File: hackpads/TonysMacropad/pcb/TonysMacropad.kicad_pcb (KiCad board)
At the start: 2 copper layers, 81 x 61.9 mm, 21 parts, among them SW1 SW_Push_45deg, SW2 SW_Push_45deg, SW3 SW_Push_45deg, SW4 SW_Push_45deg, SW5 SW_Push_45deg, SW6 SW_Push_45deg, SW7 SW_Push_45deg, SW8 SW_Push_45deg, SW9 SW_Push_45deg, U1 Seeed Studio XIAO SAMD21

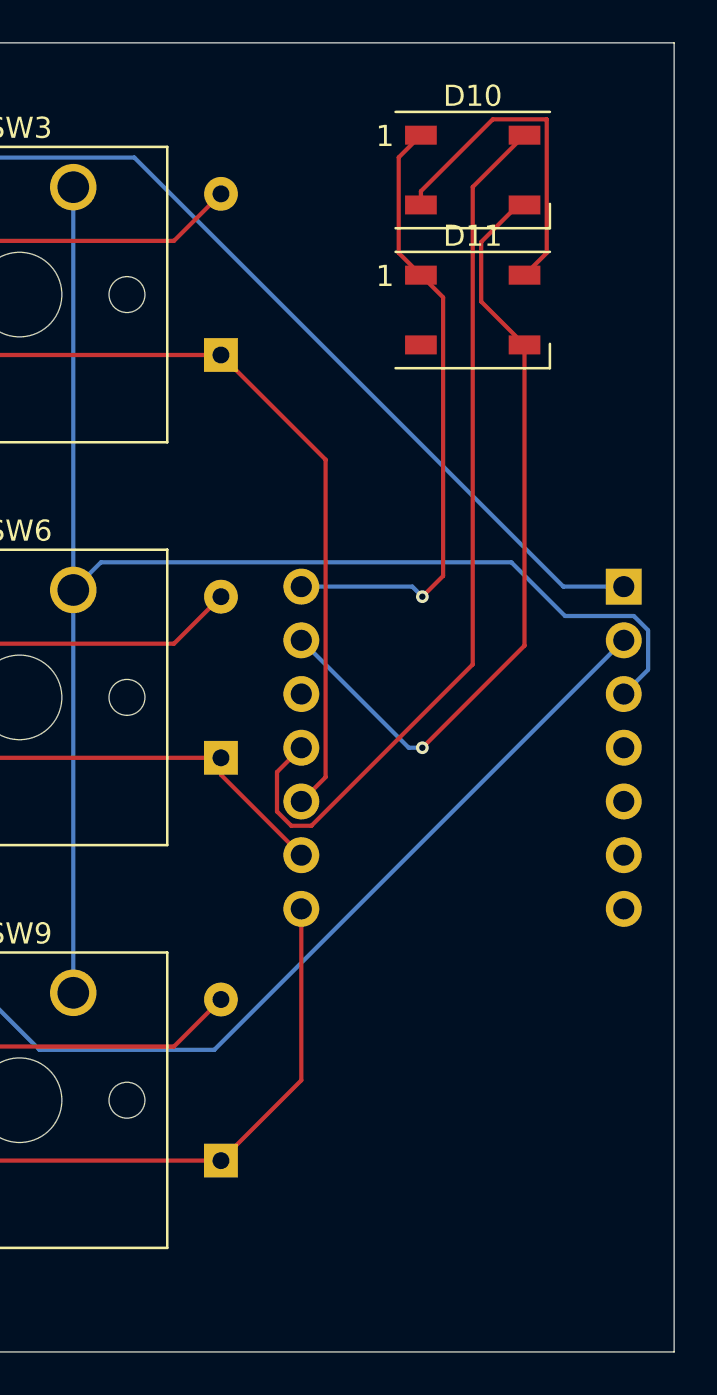
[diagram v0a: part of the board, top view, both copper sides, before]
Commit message: add two RGB leds
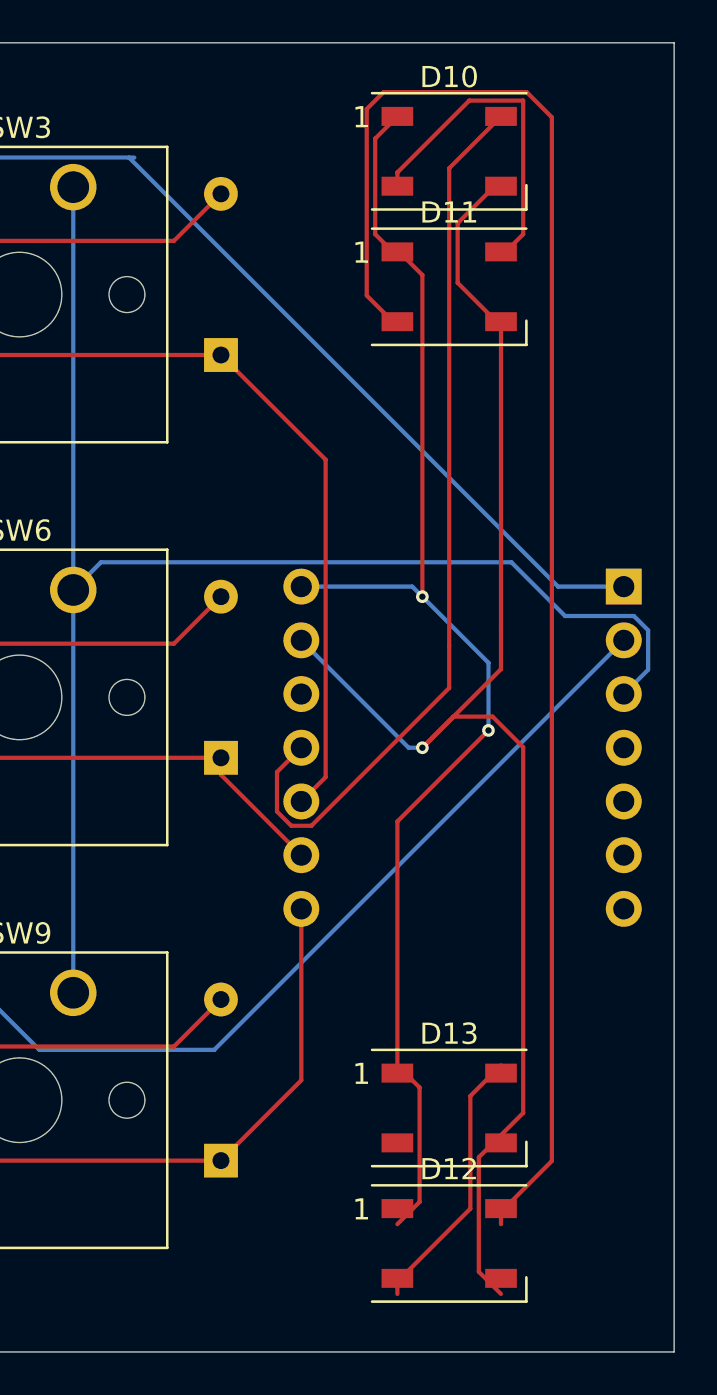
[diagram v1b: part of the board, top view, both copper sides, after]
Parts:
- added D12: WS2812B, LED_SMD:LED_WS2812B_PLCC4_5.0x5.0mm_P3.2mm, F.Cu at (144.1, 97.3)
- added D13: WS2812B, LED_SMD:LED_WS2812B_PLCC4_5.0x5.0mm_P3.2mm, F.Cu at (144.1, 90.9)
- moved D11 1.56 mm to (144.1, 52.0)
- moved D10 1.42 mm to (144.1, 45.6)
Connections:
- D11 pad 2: unconnected-(D11-DOUT-Pad2) -> Net-(D11-DOUT)
- U1 pad 5: unconnected-(U1-PA8_A4_D4_SDA-Pad5) -> SDA
- U1 pad 6: unconnected-(U1-PA9_A5_D5_SCL-Pad6) -> SCL
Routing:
- net Net-(D11-DOUT): track 0.00 -> 73.8 mm
- net VCC: track 29.5 -> 63.8 mm, vias 1 -> 2
- net GND: track 37.4 -> 70.9 mm
- net Net-(D12-DOUT): track 0.00 -> 12.8 mm

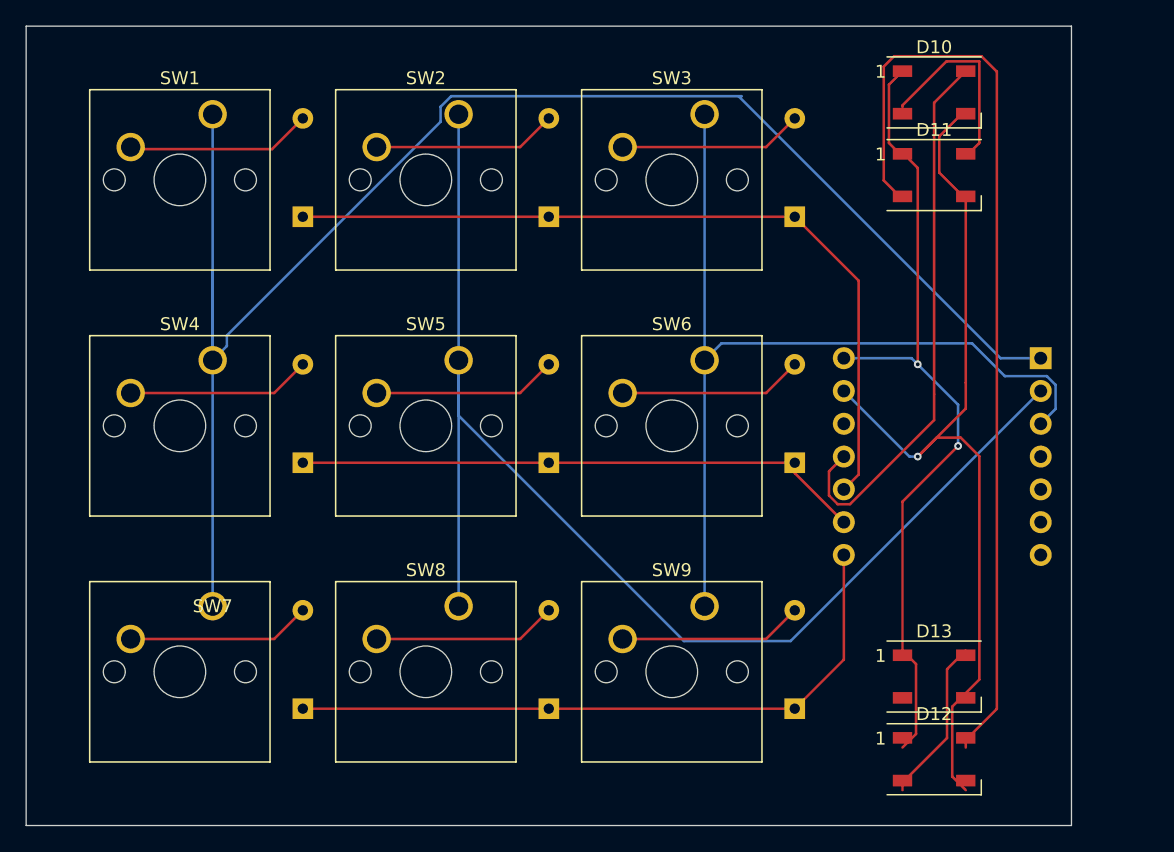
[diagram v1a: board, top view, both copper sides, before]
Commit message: fix mcu usb position
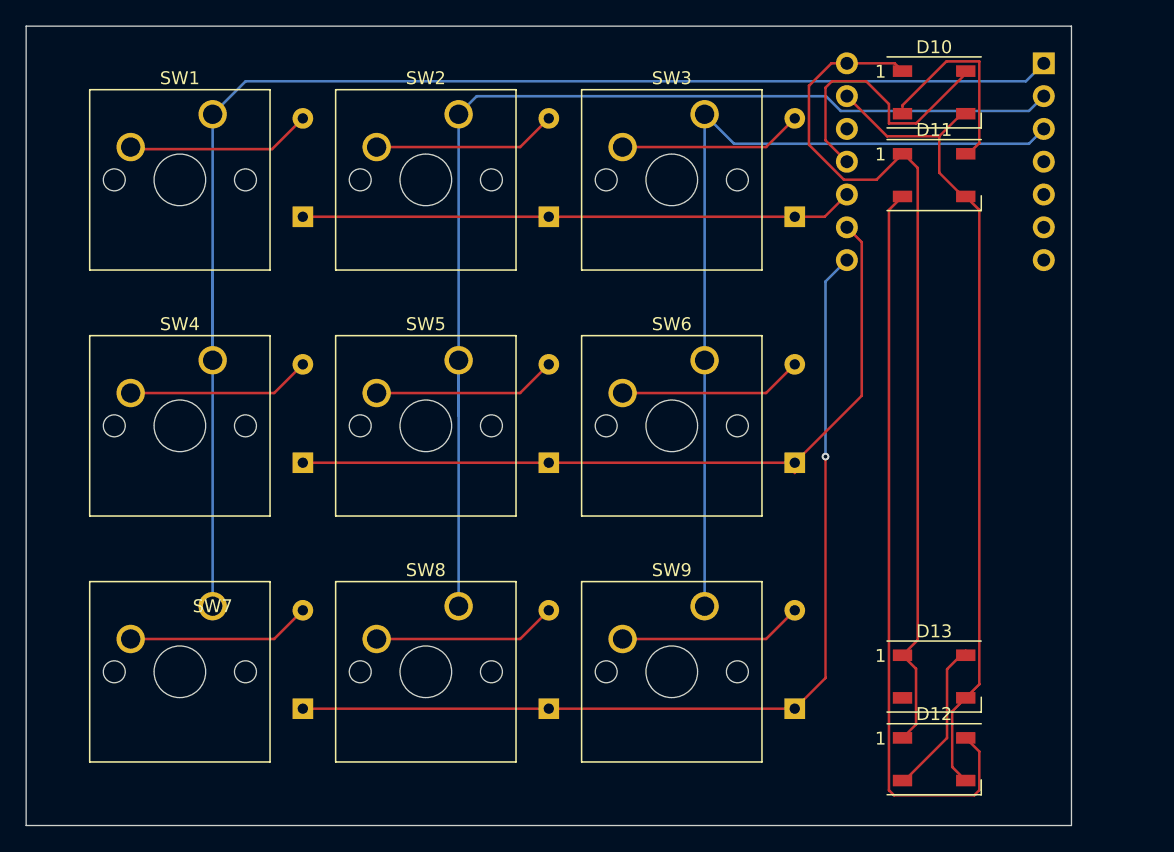
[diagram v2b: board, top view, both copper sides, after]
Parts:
- moved U1 22.8 mm to (145.0, 51.0)
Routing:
- net Row 2: track 51.6 -> 74.5 mm, vias 0 -> 1
- net WS2812B: track 42.7 -> 21.5 mm
- net Row 0: track 61.7 -> 42.9 mm
- net Col 0: track 127.5 -> 111.1 mm
- net Net-(D11-DOUT): track 73.8 -> 58.2 mm
- net Row 1: track 44.3 -> 59.8 mm
- net Col 1: track 102.7 -> 89.2 mm
- net GND: track 70.9 -> 63.9 mm, vias 1 -> 0
- net VCC: track 63.8 -> 69.0 mm, vias 2 -> 0
- net Col 2: track 70.7 -> 65.8 mm
- net Net-(D12-DOUT): track 12.8 -> 12.3 mm

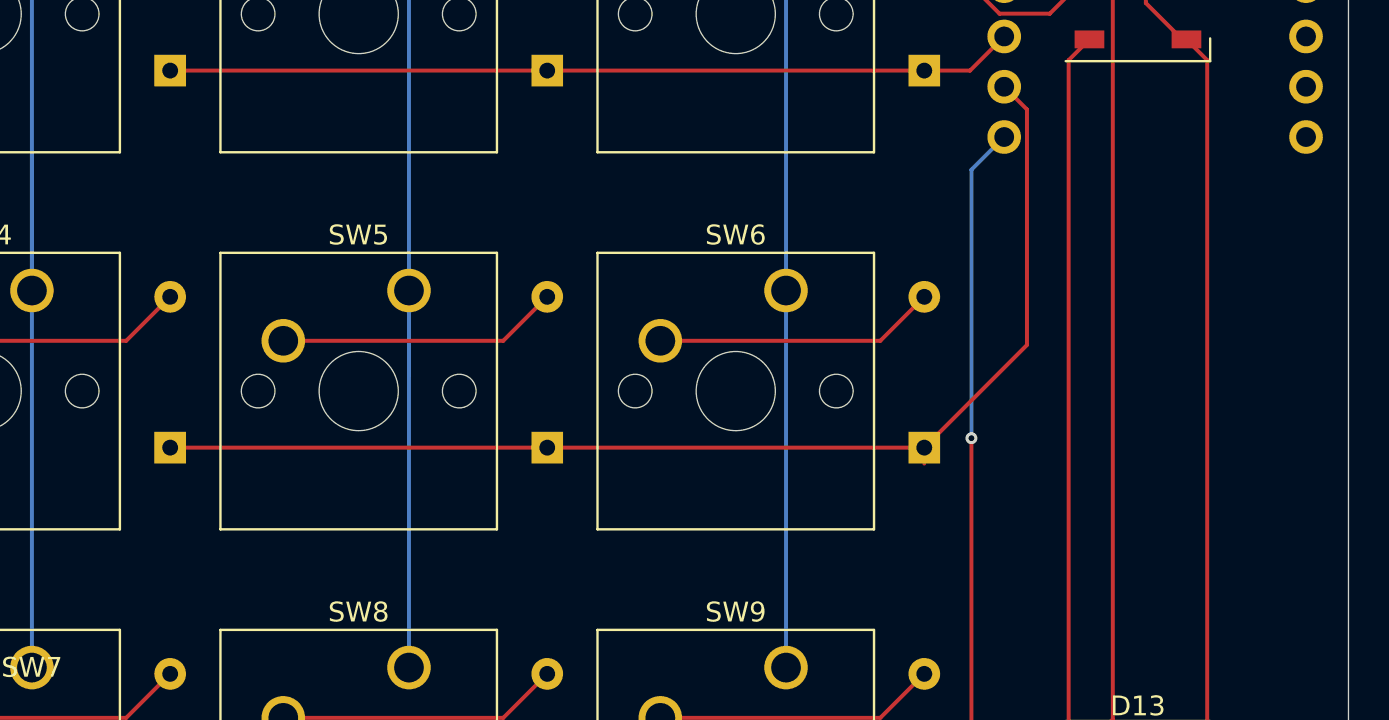
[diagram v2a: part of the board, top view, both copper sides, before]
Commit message: add mounting screws / use heatset inserts
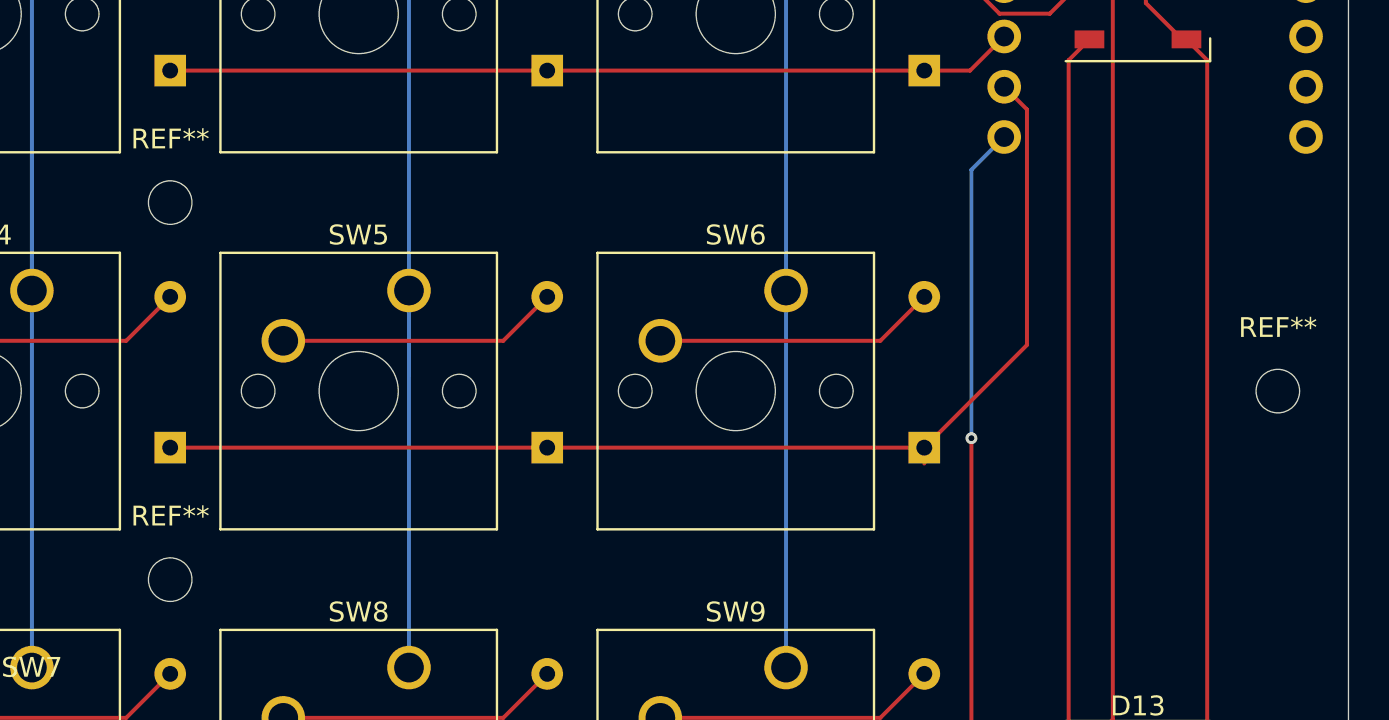
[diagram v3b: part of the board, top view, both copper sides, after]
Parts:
- added REF**: MountingHole_2.2mm_M2, MountingHole:MountingHole_2.2mm_M2, F.Cu at (95.3, 81.0)
- added REF**: MountingHole_2.2mm_M2, MountingHole:MountingHole_2.2mm_M2, F.Cu at (151.2, 71.4)
- added REF**: MountingHole_2.2mm_M2, MountingHole:MountingHole_2.2mm_M2, F.Cu at (95.3, 61.9)

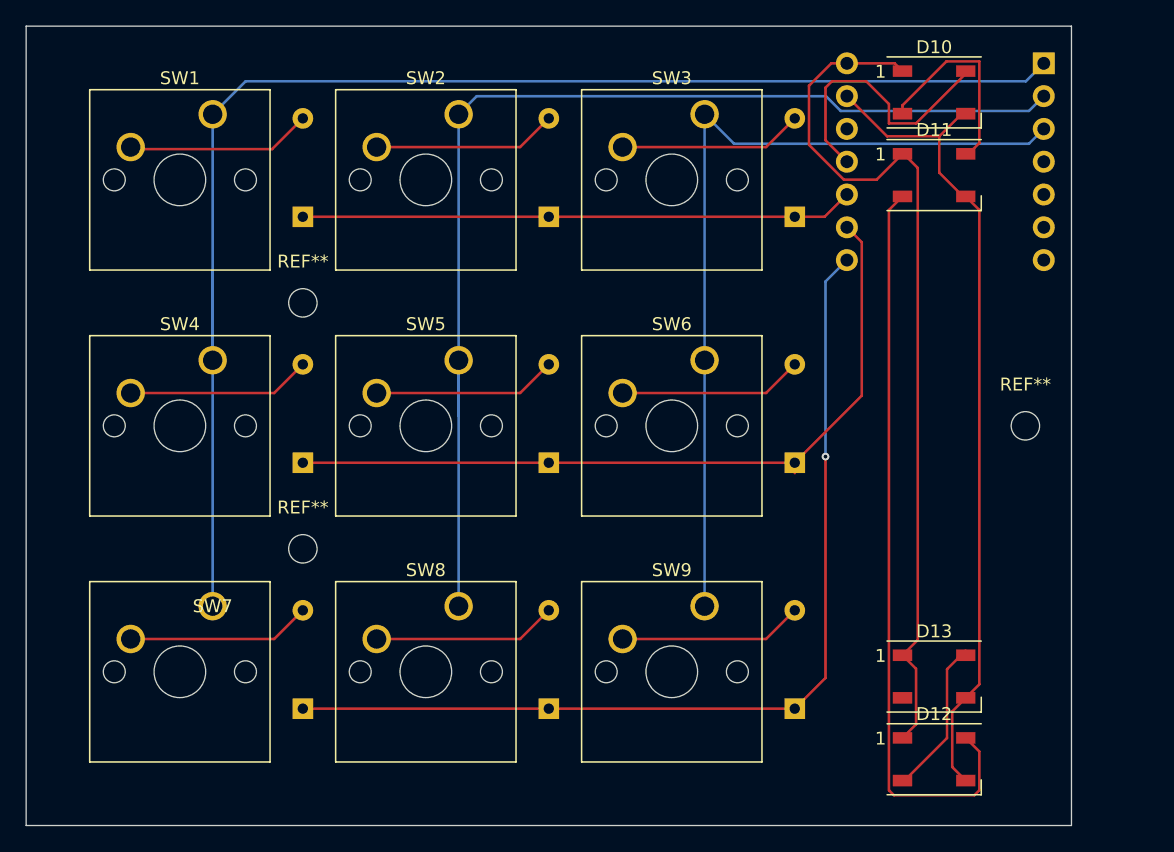
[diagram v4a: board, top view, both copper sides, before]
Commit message: add rotary encoder
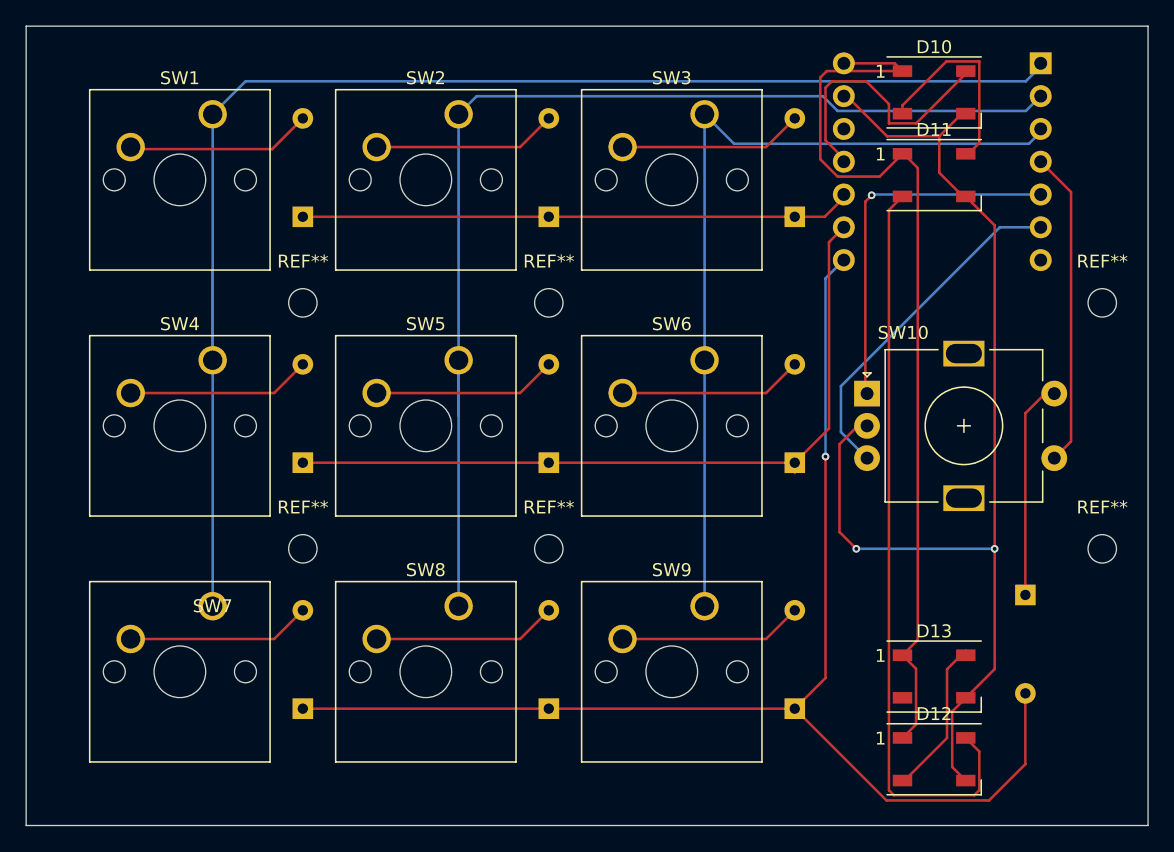
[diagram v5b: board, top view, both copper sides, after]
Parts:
- removed U1: Seeed Studio XIAO SAMD21, Seeed Studio XIAO Series Library:XIAO-Generic-Thruhole-14P-2.54-21X17.8MM
- added D14: D, Diode_THT:D_DO-35_SOD27_P7.62mm_Horizontal, B.Cu at (151.2, 84.5)
- added REF**: MountingHole_2.2mm_M2, MountingHole:MountingHole_2.2mm_M2, F.Cu at (114.3, 61.9)
- added REF**: MountingHole_2.2mm_M2, MountingHole:MountingHole_2.2mm_M2, F.Cu at (157.2, 61.9)
- added REF**: MountingHole_2.2mm_M2, MountingHole:MountingHole_2.2mm_M2, F.Cu at (157.2, 81.0)
- added SW10: RotaryEncoder_Switch, Rotary_Encoder:RotaryEncoder_Alps_EC11E-Switch_Vertical_H20mm, F.Cu at (138.9, 68.9)
- added U2: MOUDLE-SEEEDUINO-XIAO, Seeed Studio XIAO Series Library:XIAO-Generic-Thruhole-14P-2.54-21X17.8MM, B.Cu at (144.8, 51.0)
- moved REF** 38.1 mm to (114.3, 81.0)
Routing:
- net EC11A: track 0.00 -> 28.7 mm, vias 0 -> 1
- net Row 2: track 74.5 -> 101.9 mm
- net EC11B: track 0.00 -> 27.0 mm
- net EC11SWB: track 0.00 -> 24.5 mm
- net GND: track 63.9 -> 86.1 mm, vias 0 -> 2
- net EC11SWA: track 0.00 -> 16.1 mm
- net VCC: track 69.0 -> 72.2 mm
- net Row 1: track 59.8 -> 58.7 mm
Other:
- board size 81 x 61.9 mm -> 86.9 x 61.9 mm
